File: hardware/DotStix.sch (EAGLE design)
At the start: 23 parts, among them U1 ATMEGA328P-MU-QFN32

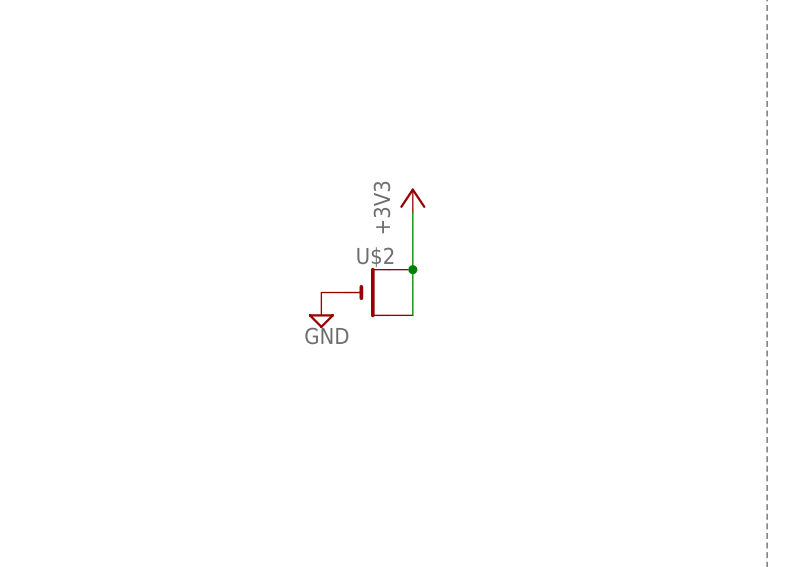
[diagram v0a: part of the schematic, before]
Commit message: Add 100uF cap
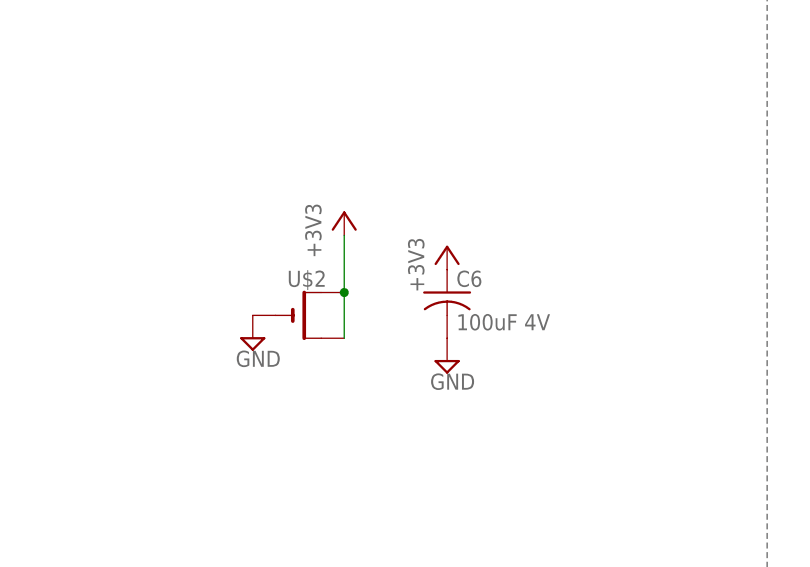
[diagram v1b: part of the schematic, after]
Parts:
- added C6: 100uF 4V, adafruit:C-USC3216
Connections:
- net +3V3: now also C6.1
- net GND: now also C6.2
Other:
- moved on the sheet: U$2
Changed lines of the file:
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@@
 <setting verticaltext="up"/>
 </settings>
-<grid distance="0.05" unitdist="inch" unit="inch" style="lines" multiple="1" display="no" altdistance="0.01" altunitdist="inch" altunit="inch"/>
+<grid distance="0.1" unitdist="inch" unit="inch" style="lines" multiple="1" display="no" altdistance="0.01" altunitdist="inch" altunit="inch"/>
 <layers>
 <layer number="1" name="Top" color="4" fill="1" visible="no" active="no"/>
@@
 <part name="R5" library="resistor" deviceset="R-EU_" device="R0603" value="&gt;1MΩ"/>
 <part name="+3V8" library="supply1" deviceset="+3V3" device=""/>
+<part name="+3V10" library="supply1" deviceset="+3V3" device=""/>
+<part name="SUPPLY16" library="supply2" deviceset="GND" device=""/>
+<part name="C6" library="adafruit" deviceset="C-US" device="C3216" value="100uF 4V"/>
 </parts>
 <sheets>
@@
 <instance part="R1" gate="C" x="40.64" y="163.83" rot="R90"/>
 <instance part="R1" gate="D" x="15.24" y="163.83" rot="R90"/>
-<instance part="U$2" gate="G$1" x="267.97" y="157.48"/>
-<instance part="+3V1" gate="G$1" x="273.05" y="168.91"/>
-<instance part="SUPPLY1" gate="GND" x="262.89" y="154.94"/>
+<instance part="U$2" gate="G$1" x="260.35" y="154.94"/>
+<instance part="+3V1" gate="G$1" x="265.43" y="166.37"/>
+<instance part="SUPPLY1" gate="GND" x="255.27" y="152.4"/>
 <instance part="R2" gate="G$1" x="71.12" y="162.56" rot="R90"/>
 <instance part="+3V6" gate="G$1" x="71.12" y="172.72"/>
@@
 <instance part="R5" gate="G$1" x="78.74" y="71.12" rot="R90"/>
 <instance part="+3V8" gate="G$1" x="78.74" y="78.74"/>
+<instance part="+3V10" gate="G$1" x="276.86" y="162.56"/>
+<instance part="SUPPLY16" gate="GND" x="276.86" y="149.86"/>
+<instance part="C6" gate="G$1" x="276.86" y="157.48"/>
 </instances>
 <busses>
@@
 <wire x1="1.27" y1="35.56" x2="1.27" y2="34.29" width="0.1524" layer="91"/>
 </segment>
+<segment>
+<pinref part="SUPPLY16" gate="GND" pin="GND"/>
+<pinref part="C6" gate="G$1" pin="2"/>
+</segment>
 </net>
 <net name="SDA" class="0">
@@
 <pinref part="+3V1" gate="G$1" pin="+3V3"/>
 <pinref part="U$2" gate="G$1" pin="+"/>
-<wire x1="273.05" y1="166.37" x2="273.05" y2="160.02" width="0.1524" layer="91"/>
+<wire x1="265.43" y1="163.83" x2="265.43" y2="157.48" width="0.1524" layer="91"/>
 <pinref part="U$2" gate="G$1" pin="+1"/>
-<wire x1="273.05" y1="160.02" x2="273.05" y2="154.94" width="0.1524" layer="91"/>
-<junction x="273.05" y="160.02"/>
+<wire x1="265.43" y1="157.48" x2="265.43" y2="152.4" width="0.1524" layer="91"/>
+<junction x="265.43" y="157.48"/>
 </segment>
 <segment>
@@
 <pinref part="+3V8" gate="G$1" pin="+3V3"/>
 </segment>
-</net>
+<segment>
+<pinref part="+3V10" gate="G$1" pin="+3V3"/>
+<pinref part="C6" gate="G$1" pin="1"/>
+</segment>
+</net>

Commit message: Exp: Add Temp & UV sensors
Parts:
- removed R1: (no value), SparkFun:RESISTOR-ARRAY0603-ARV
- removed R2: (no value), resistor:R-EU_R0603
- added IC2: SI1145, silabs:SI1145
- added RN1, RN2: (no value), resistor-dil:4R-N0402ARV341
- added SJ1: SOLDERJUMPERTRACE, SparkFun:SOLDERJUMPERTRACE
- added U2: TMP102, SparkFun:TMP102
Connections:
- new net INT_MULTIPLE: IC2.INT, U1.PD7(AIN1/PCINT23), U2.ALERT
- new net N$5: RN1A.2, SJ1.1
- net +3V3: now also IC2.VDD, RN1B.2, RN1C.2, RN1D.2, SJ1.2, U2.VCC; no longer R2.2
- net GND: now also IC2.GND, U2.ADD0, U2.GND
- net LED_BLUE: now also RN2B.1; no longer R1B.1
- net LED_GREEN: now also RN2A.1; no longer R1A.1
- net LED_RED: now also RN2C.1; no longer R1C.1
- net N$1: now also RN2B.2; no longer R1B.2
- net N$3: now also RN2A.2; no longer R1A.2
- net N$4: now also RN2C.2; no longer R1C.2
- net RST: no longer R2.1
- net SCL: now also IC2.SCL, U2.SCL
- net SDA: now also IC2.SDA, U2.SDA
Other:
- note added: "TMP102 or TMP112 (high acc +/-0.5°)"
- moved on the sheet: LED2

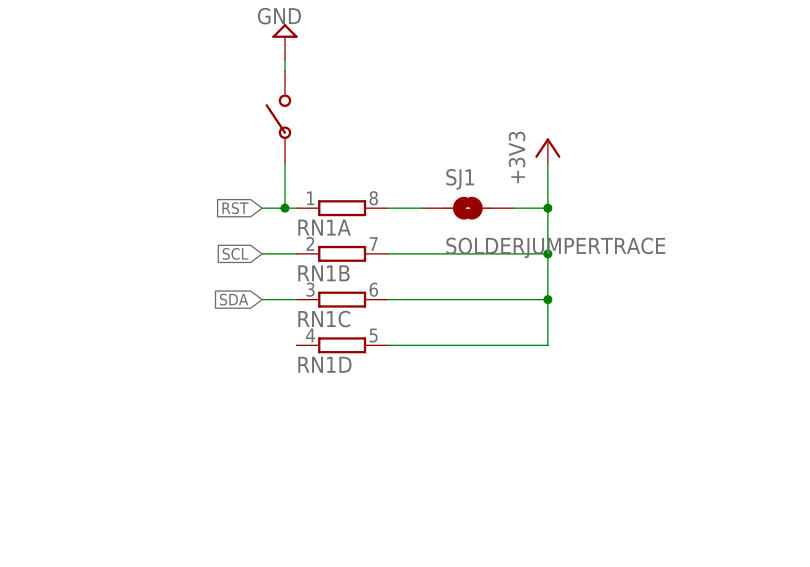
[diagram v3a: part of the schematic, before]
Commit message: Fix unconnected 4.7k pullups
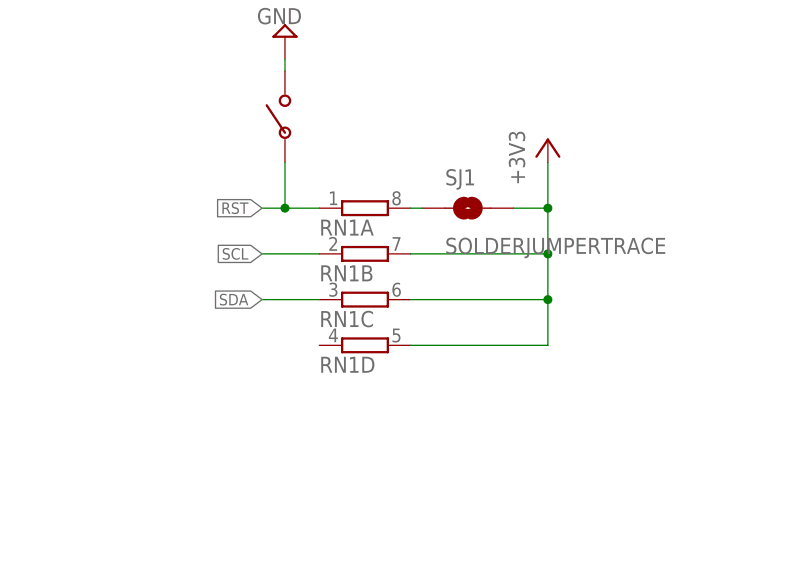
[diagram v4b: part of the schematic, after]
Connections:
- net RST: now also RN1A.1
- net SCL: now also RN1B.1
- net SDA: now also RN1C.1
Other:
- moved on the sheet: RN1A, RN1B, RN1C, RN1D
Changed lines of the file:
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@@
 <setting verticaltext="up"/>
 </settings>
-<grid distance="0.1" unitdist="inch" unit="inch" style="lines" multiple="1" display="no" altdistance="0.01" altunitdist="inch" altunit="inch"/>
+<grid distance="0.05" unitdist="inch" unit="inch" style="lines" multiple="1" display="no" altdistance="0.01" altunitdist="inch" altunit="inch"/>
 <layers>
 <layer number="1" name="Top" color="4" fill="1" visible="no" active="no"/>
@@
 <instance part="SJ1" gate="1" x="88.9" y="148.59"/>
 <instance part="U$3" gate="G$1" x="68.58" y="158.75" rot="R90"/>
-<instance part="RN1" gate="A" x="74.93" y="148.59"/>
-<instance part="RN1" gate="B" x="74.93" y="143.51"/>
-<instance part="RN1" gate="C" x="74.93" y="138.43"/>
-<instance part="RN1" gate="D" x="74.93" y="133.35"/>
+<instance part="RN1" gate="A" x="77.47" y="148.59"/>
+<instance part="RN1" gate="B" x="77.47" y="143.51"/>
+<instance part="RN1" gate="C" x="77.47" y="138.43"/>
+<instance part="RN1" gate="D" x="77.47" y="133.35"/>
 <instance part="RN2" gate="A" x="12.7" y="140.97" rot="R90"/>
 <instance part="RN2" gate="B" x="7.62" y="140.97" rot="R90"/>
@@
 </segment>
 <segment>
-<wire x1="69.85" y1="138.43" x2="66.04" y2="138.43" width="0.1524" layer="91"/>
+<wire x1="72.39" y1="138.43" x2="66.04" y2="138.43" width="0.1524" layer="91"/>
 <label x="66.04" y="138.43" size="1.27" layer="95" rot="R180" xref="yes"/>
+<pinref part="RN1" gate="C" pin="1"/>
 </segment>
 <segment>
@@
 </segment>
 <segment>
-<wire x1="69.85" y1="148.59" x2="68.58" y2="148.59" width="0.1524" layer="91"/>
 <label x="66.04" y="148.59" size="1.27" layer="95" rot="R180" xref="yes"/>
 <pinref part="U$3" gate="G$1" pin="P$1"/>
@@
 <wire x1="68.58" y1="153.67" x2="68.58" y2="148.59" width="0.1524" layer="91"/>
 <junction x="68.58" y="148.59"/>
+<pinref part="RN1" gate="A" pin="1"/>
+<wire x1="72.39" y1="148.59" x2="68.58" y2="148.59" width="0.1524" layer="91"/>
 </segment>
 </net>
@@
 <wire x1="97.79" y1="143.51" x2="97.79" y2="148.59" width="0.1524" layer="91"/>
 <wire x1="97.79" y1="148.59" x2="97.79" y2="153.67" width="0.1524" layer="91"/>
-<wire x1="80.01" y1="143.51" x2="97.79" y2="143.51" width="0.1524" layer="91"/>
+<wire x1="82.55" y1="143.51" x2="97.79" y2="143.51" width="0.1524" layer="91"/>
 <junction x="97.79" y="143.51"/>
-<wire x1="80.01" y1="138.43" x2="97.79" y2="138.43" width="0.1524" layer="91"/>
+<wire x1="82.55" y1="138.43" x2="97.79" y2="138.43" width="0.1524" layer="91"/>
 <junction x="97.79" y="138.43"/>
-<wire x1="80.01" y1="133.35" x2="97.79" y2="133.35" width="0.1524" layer="91"/>
+<wire x1="82.55" y1="133.35" x2="97.79" y2="133.35" width="0.1524" layer="91"/>
 <pinref part="SJ1" gate="1" pin="2"/>
 <wire x1="93.98" y1="148.59" x2="97.79" y2="148.59" width="0.1524" layer="91"/>
@@
 </segment>
 <segment>
-<wire x1="69.85" y1="143.51" x2="66.04" y2="143.51" width="0.1524" layer="91"/>
+<wire x1="72.39" y1="143.51" x2="66.04" y2="143.51" width="0.1524" layer="91"/>
 <label x="66.04" y="143.51" size="1.27" layer="95" rot="R180" xref="yes"/>
+<pinref part="RN1" gate="B" pin="1"/>
 </segment>
 <segment>
@@
 <segment>
 <pinref part="SJ1" gate="1" pin="1"/>
-<wire x1="83.82" y1="148.59" x2="80.01" y2="148.59" width="0.1524" layer="91"/>
+<wire x1="83.82" y1="148.59" x2="82.55" y2="148.59" width="0.1524" layer="91"/>
 <pinref part="RN1" gate="A" pin="2"/>
 </segment>

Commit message: Draft: add 9DoF motion sensor
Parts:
- added C8: 0.1uF, resistor:C-EUC0603
- added U4: 9DoF IMU, SparkFun-Sensors:MPU-9250
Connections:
- new net N$11: C8.1, U4.REGOUT
- net +3V3: now also U4.VDD, U4.VDDIO
- net GND: now also C8.2, U4.AD0/SDO, U4.FSYNC, U4.GND
- net INT_MULTIPLE: now also RN1D.1, U4.INT
- net SCL: now also U4.SCL/SCLK
- net SDA: now also U4.SDA/SDI
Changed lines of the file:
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@@
 <part name="+3V12" library="supply1" deviceset="+3V3" device=""/>
 <part name="SUPPLY7" library="supply2" deviceset="GND" device=""/>
+<part name="U4" library="SparkFun-Sensors" deviceset="MPU-9250" device="" value="9DoF IMU"/>
+<part name="SUPPLY23" library="supply2" deviceset="GND" device=""/>
+<part name="SUPPLY24" library="supply2" deviceset="GND" device=""/>
+<part name="C8" library="resistor" deviceset="C-EU" device="C0603" value="0.1uF"/>
+<part name="SUPPLY25" library="supply2" deviceset="GND" device=""/>
+<part name="+3V13" library="supply1" deviceset="+3V3" device=""/>
+<part name="SUPPLY28" library="supply2" deviceset="GND" device=""/>
 </parts>
 <sheets>
@@
 <instance part="+3V12" gate="G$1" x="384.81" y="166.37"/>
 <instance part="SUPPLY7" gate="GND" x="417.83" y="151.13"/>
+<instance part="U4" gate="G$1" x="435.61" y="123.19"/>
+<instance part="SUPPLY23" gate="GND" x="417.83" y="115.57"/>
+<instance part="SUPPLY24" gate="GND" x="453.39" y="115.57"/>
+<instance part="C8" gate="G$1" x="407.67" y="118.11"/>
+<instance part="SUPPLY25" gate="GND" x="407.67" y="110.49"/>
+<instance part="+3V13" gate="G$1" x="389.89" y="133.35"/>
+<instance part="SUPPLY28" gate="GND" x="402.59" y="115.57"/>
 </instances>
 <busses>
@@
 <pinref part="SUPPLY7" gate="GND" pin="GND"/>
 </segment>
+<segment>
+<pinref part="C8" gate="G$1" pin="2"/>
+<pinref part="SUPPLY25" gate="GND" pin="GND"/>
+</segment>
+<segment>
+<pinref part="U4" gate="G$1" pin="GND"/>
+<pinref part="SUPPLY23" gate="GND" pin="GND"/>
+</segment>
+<segment>
+<pinref part="U4" gate="G$1" pin="FSYNC"/>
+<wire x1="417.83" y1="123.19" x2="402.59" y2="123.19" width="0.1524" layer="91"/>
+<wire x1="402.59" y1="123.19" x2="402.59" y2="118.11" width="0.1524" layer="91"/>
+<pinref part="SUPPLY28" gate="GND" pin="GND"/>
+</segment>
+<segment>
+<pinref part="U4" gate="G$1" pin="AD0/SDO"/>
+<pinref part="SUPPLY24" gate="GND" pin="GND"/>
+</segment>
 </net>
 <net name="SDA" class="0">
@@
 <wire x1="417.83" y1="163.83" x2="420.37" y2="163.83" width="0.1524" layer="91"/>
 <label x="420.37" y="163.83" size="1.27" layer="95" xref="yes"/>
+</segment>
+<segment>
+<pinref part="U4" gate="G$1" pin="SDA/SDI"/>
+<wire x1="453.39" y1="120.65" x2="455.93" y2="120.65" width="0.1524" layer="91"/>
+<label x="455.93" y="120.65" size="1.27" layer="95" xref="yes"/>
 </segment>
 </net>
@@
 <pinref part="U2" gate="G$1" pin="VCC"/>
 </segment>
+<segment>
+<pinref part="+3V13" gate="G$1" pin="+3V3"/>
+<pinref part="U4" gate="G$1" pin="VDD"/>
+<wire x1="389.89" y1="130.81" x2="415.29" y2="130.81" width="0.1524" layer="91"/>
+<pinref part="U4" gate="G$1" pin="VDDIO"/>
+<wire x1="415.29" y1="130.81" x2="417.83" y2="130.81" width="0.1524" layer="91"/>
+<wire x1="417.83" y1="128.27" x2="415.29" y2="128.27" width="0.1524" layer="91"/>
+<wire x1="415.29" y1="128.27" x2="415.29" y2="130.81" width="0.1524" layer="91"/>
+<junction x="415.29" y="130.81"/>
+</segment>
 </net>
 <net name="MOSI" class="0">
@@
 <wire x1="417.83" y1="161.29" x2="420.37" y2="161.29" width="0.1524" layer="91"/>
 <label x="420.37" y="161.29" size="1.27" layer="95" xref="yes"/>
+</segment>
+<segment>
+<pinref part="U4" gate="G$1" pin="SCL/SCLK"/>
+<wire x1="453.39" y1="123.19" x2="455.93" y2="123.19" width="0.1524" layer="91"/>
+<label x="455.93" y="123.19" size="1.27" layer="95" xref="yes"/>
 </segment>
 </net>
@@
 <label x="198.12" y="20.32" size="1.27" layer="95" xref="yes"/>
 </segment>
-</net>
+<segment>
+<pinref part="RN1" gate="D" pin="1"/>
+<wire x1="72.39" y1="133.35" x2="66.04" y2="133.35" width="0.1524" layer="91"/>
+<label x="66.04" y="133.35" size="1.27" layer="95" rot="R180" xref="yes"/>
+</segment>
+<segment>
+<pinref part="U4" gate="G$1" pin="INT"/>
+<wire x1="417.83" y1="125.73" x2="415.29" y2="125.73" width="0.1524" layer="91"/>
+<label x="415.29" y="125.73" size="1.27" layer="95" rot="R180" xref="yes"/>
+</segment>
+</net>
+<net name="N$11" class="0">
+<segment>
+<pinref part="U4" gate="G$1" pin="REGOUT"/>
+<pinref part="C8" gate="G$1" pin="1"/>
+<wire x1="417.83" y1="120.65" x2="407.67" y2="120.65" width="0.1524" layer="91"/>
+</segment>
+</net>

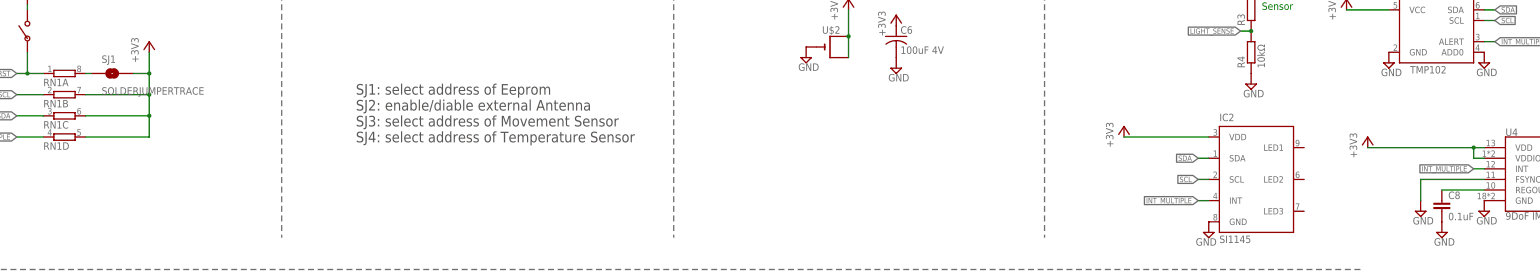
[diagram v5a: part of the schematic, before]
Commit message: Draft:  9DoF pins connected, need to fix warnings
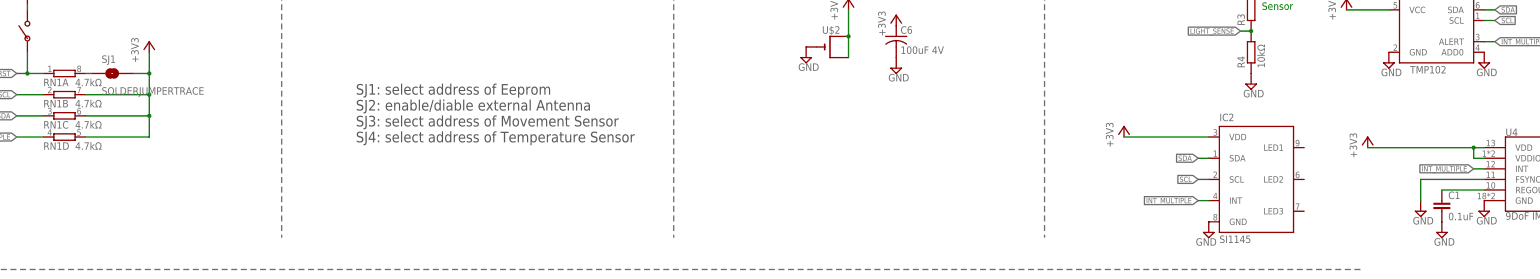
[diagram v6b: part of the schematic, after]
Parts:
- removed C8: 0.1uF, resistor:C-EUC0603
- added C1: 0.1uF, rcl:C-EUC0201
- RN1: value (none) -> 4.7kΩ
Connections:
- net GND: now also C1.2; no longer C8.2
- net N$11: now also C1.1; no longer C8.1
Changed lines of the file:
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@@
 <part name="SJ1" library="SparkFun" deviceset="SOLDERJUMPER" device="TRACE"/>
 <part name="U$3" library="pusbbutton_4x2_5" deviceset="PUSHBUTTON_4X2.5" device=""/>
-<part name="RN1" library="resistor-dil" deviceset="4R-N" device="0402ARV341"/>
+<part name="RN1" library="resistor-dil" deviceset="4R-N" device="0402ARV341" value="4.7kΩ"/>
 <part name="RN2" library="resistor-dil" deviceset="4R-N" device="0402ARV341"/>
 <part name="IC2" library="silabs" deviceset="SI114*" device="" technology="5"/>
@@
 <part name="SUPPLY23" library="supply2" deviceset="GND" device=""/>
 <part name="SUPPLY24" library="supply2" deviceset="GND" device=""/>
-<part name="C8" library="resistor" deviceset="C-EU" device="C0603" value="0.1uF"/>
 <part name="SUPPLY25" library="supply2" deviceset="GND" device=""/>
 <part name="+3V13" library="supply1" deviceset="+3V3" device=""/>
 <part name="SUPPLY28" library="supply2" deviceset="GND" device=""/>
+<part name="C1" library="rcl" deviceset="C-EU" device="C0201" value="0.1uF"/>
 </parts>
 <sheets>
@@
 <instance part="SUPPLY23" gate="GND" x="417.83" y="115.57"/>
 <instance part="SUPPLY24" gate="GND" x="453.39" y="115.57"/>
-<instance part="C8" gate="G$1" x="407.67" y="118.11"/>
 <instance part="SUPPLY25" gate="GND" x="407.67" y="110.49"/>
 <instance part="+3V13" gate="G$1" x="389.89" y="133.35"/>
 <instance part="SUPPLY28" gate="GND" x="402.59" y="115.57"/>
+<instance part="C1" gate="G$1" x="407.67" y="118.11"/>
 </instances>
 <busses>
@@
 </segment>
 <segment>
-<pinref part="C8" gate="G$1" pin="2"/>
-<pinref part="SUPPLY25" gate="GND" pin="GND"/>
-</segment>
-<segment>
 <pinref part="U4" gate="G$1" pin="GND"/>
 <pinref part="SUPPLY23" gate="GND" pin="GND"/>
@@
 <pinref part="U4" gate="G$1" pin="AD0/SDO"/>
 <pinref part="SUPPLY24" gate="GND" pin="GND"/>
+</segment>
+<segment>
+<pinref part="SUPPLY25" gate="GND" pin="GND"/>
+<pinref part="C1" gate="G$1" pin="2"/>
 </segment>
 </net>
@@
 <segment>
 <pinref part="U4" gate="G$1" pin="REGOUT"/>
-<pinref part="C8" gate="G$1" pin="1"/>
 <wire x1="417.83" y1="120.65" x2="407.67" y2="120.65" width="0.1524" layer="91"/>
-</segment>
-</net>
+<pinref part="C1" gate="G$1" pin="1"/>
+</segment>
+</net>
